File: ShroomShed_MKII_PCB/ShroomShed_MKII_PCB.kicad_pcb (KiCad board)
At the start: 4 copper layers, 91 x 72 mm, 92 parts, among them J1 TYPE-C-31-M-12, J2 UART, J3 Inputs, J4 SHT31, J5 SWD 14 pin header, J6 ERM, J7 SD_SPI, J8 Display_Touch_SPI, Q1 BC817, SW1 EVQ-Q2B03W, SW2 BOOT SELECT, U1 WS2811, U2 WS2811, U3 TPS61085DGK, U4 USBLC6-2SC6, U5 WS2811, U6 WS2811, U7 ENS210, U8 AMS1117-3.3, U9 STM32H562VGTx, Y1 16MHz

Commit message: completed controler V2.2, got basic blocking implementation of display SPI DMA working
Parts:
- removed the C12 at (173.7, 80.7)
- removed the R12 at (170.5, 77.9)
- removed the R13 at (176.4, 78.7)
- removed the U7 at (173.8, 78.4)
- added J10: GPIO_GND, Connector_PinHeader_2.54mm:PinHeader_2x02_P2.54mm_Vertical, F.Cu at (180.0, 67.2)
- added J4: GPIO_PWR, Connector_PinHeader_2.54mm:PinHeader_2x03_P2.54mm_Vertical, F.Cu at (169.2, 83.6)
- C14: renamed from C15; value 100uF -> 220uF
- H1, H2, H3, H4: footprint MountingHole:MountingHole_3.2mm_M3_Pad -> MountingHole:MountingHole_3.2mm_M3_Pad_Via
- J2: value UART -> GPIO_1; footprint Connector_PinHeader_2.00mm:PinHeader_1x04_P2.00mm_Vertical -> Connector_PinHeader_2.54mm:PinHeader_2x08_P2.54mm_Vertical
- J3: value Inputs -> GPIO_2; footprint Connector_JST:JST_XH_B6B-XH-A_1x06_P2.50mm_Vertical -> Connector_PinHeader_2.54mm:PinHeader_2x05_P2.54mm_Vertical
- moved D15 16.5 mm to (167.6, 61.0)
- moved R19 16.5 mm to (167.6, 63.0)
- moved J2 16.3 mm to (142.5, 74.0)
- moved J3 12.2 mm to (154.9, 83.6), turned to 90 degrees
- moved J6 9.90 mm to (181.7, 82.0)
- moved C2 9.01 mm to (173.0, 120.8)
- moved R1 9.01 mm to (173.0, 124.5)
- moved R3 9.01 mm to (173.0, 122.5)
- moved U1 9.01 mm to (167.2, 122.8)
- moved D1 9.01 mm to (177.8, 115.8)
- moved D2 9.01 mm to (172.0, 115.8)
- moved D3 9.01 mm to (166.2, 115.8)
- moved H1 9.00 mm to (181.0, 62.0)
- moved H3 9.00 mm to (181.0, 124.0)
- moved C15 8.62 mm to (175.6, 73.0), turned to -90 degrees
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- renumbered C13 to C12, C14 to C13, C16 to C15, C17 to C16, C18 to C17, C19 to C18, C20 to C19, C21 to C20, C22 to C21, C23 to C22, C24 to C23, C25 to C24, C26 to C25, C27 to C26, C28 to C27, J4 to J5, J5 to J7, J7 to J8, J8 to J9, R14 to R12, R15 to R13, R16 to R14, R17 to R15, R18 to R16, R19 to R17, R20 to R18, R21 to R19, U8 to U7, U9 to U8
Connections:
- J2 pad 1: +3V3 -> PA10
- J2 pad 2: RF_TX -> PA9
- J2 pad 3: RF_RX -> PC8
- J2 pad 4: GND -> PC7
- J3 pad 1: ENCODER_CHANNEL_A -> PB10
- J3 pad 2: ENCODER_CHANNEL_B -> PE15
- J3 pad 3: INPUT_1 -> PE14
- J3 pad 4: INPUT_2 -> PE13
- J3 pad 5: INPUT_3 -> PE12
- J3 pad 6: GND -> PE11
- U8 pad 38: RF_RX -> PE7
- U8 pad 39: RF_TX -> PE8
- U8 pad 40: unconnected-(U9-PE9-Pad40) -> PE9
- U8 pad 41: unconnected-(U9-PE10-Pad41) -> PE10
- U8 pad 42: unconnected-(U9-PE11-Pad42) -> PE11
- U8 pad 43: unconnected-(U9-PE12-Pad43) -> PE12
- U8 pad 44: unconnected-(U9-PE13-Pad44) -> PE13
- U8 pad 45: unconnected-(U9-PE14-Pad45) -> PE14
- U8 pad 46: unconnected-(U9-PE15-Pad46) -> PE15
- U8 pad 47: ENS210_SCL -> PB10
- U8 pad 51: ENS210_SDA -> PB12
- U8 pad 53: unconnected-(U9-PB14-Pad53) -> PB14
- U8 pad 54: unconnected-(U9-PB15-Pad54) -> PB15
- U8 pad 55: unconnected-(U9-PD8-Pad55) -> PD8
- U8 pad 56: INPUT_3 -> PD9
- U8 pad 57: INPUT_2 -> PD10
- U8 pad 58: INPUT_1 -> PD11
- U8 pad 59: ENCODER_CHANNEL_B -> PD12
- U8 pad 60: ENCODER_CHANNEL_A -> PD13
- U8 pad 61: unconnected-(U9-PD14-Pad61) -> PD14
- U8 pad 62: unconnected-(U9-PD15-Pad62) -> PD15
- U8 pad 63: unconnected-(U9-PC6-Pad63) -> PC6
- U8 pad 64: unconnected-(U9-PC7-Pad64) -> PC7
- U8 pad 65: unconnected-(U9-PC8-Pad65) -> PC8
- U8 pad 68: unconnected-(U9-PA9-Pad68) -> PA9
- U8 pad 69: unconnected-(U9-PA10-Pad69) -> PA10
- U8 pad 77: TOUCH_NSS -> unconnected-(U8-PA15(JTDI)-Pad77)
- U8 pad 93: unconnected-(U9-PB7-Pad93) -> TOUCH_NSS
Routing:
- net ENS210_SCL: track 39.8 -> 0.00 mm
- net ENS210_SDA: track 30.3 -> 0.00 mm
- net PE7: track 0.00 -> 26.5 mm, vias 0 -> 1
- net PB12: track 0.00 -> 26.0 mm
- net RGB_MOSI: track 75.0 -> 49.8 mm, vias 0 -> 2
- net PB15: track 0.00 -> 25.0 mm, vias 0 -> 1
- net PE9: track 0.00 -> 23.5 mm, vias 0 -> 1
- net PD9: track 0.00 -> 23.3 mm, vias 0 -> 1
- net INPUT_3: track 22.9 -> 0.00 mm
- net PE8: track 0.00 -> 22.8 mm
- net PB14: track 0.00 -> 22.5 mm
- net PD11: track 0.00 -> 21.5 mm, vias 0 -> 1
- net INPUT_2: track 21.1 -> 0.00 mm
- net PD8: track 0.00 -> 20.7 mm
- net PE11: track 0.00 -> 20.6 mm, vias 0 -> 1
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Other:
- board size 91 x 72 mm -> 82 x 72 mm
- board text added: "Controller V2.2"
- board text removed: "Controller V2.1"

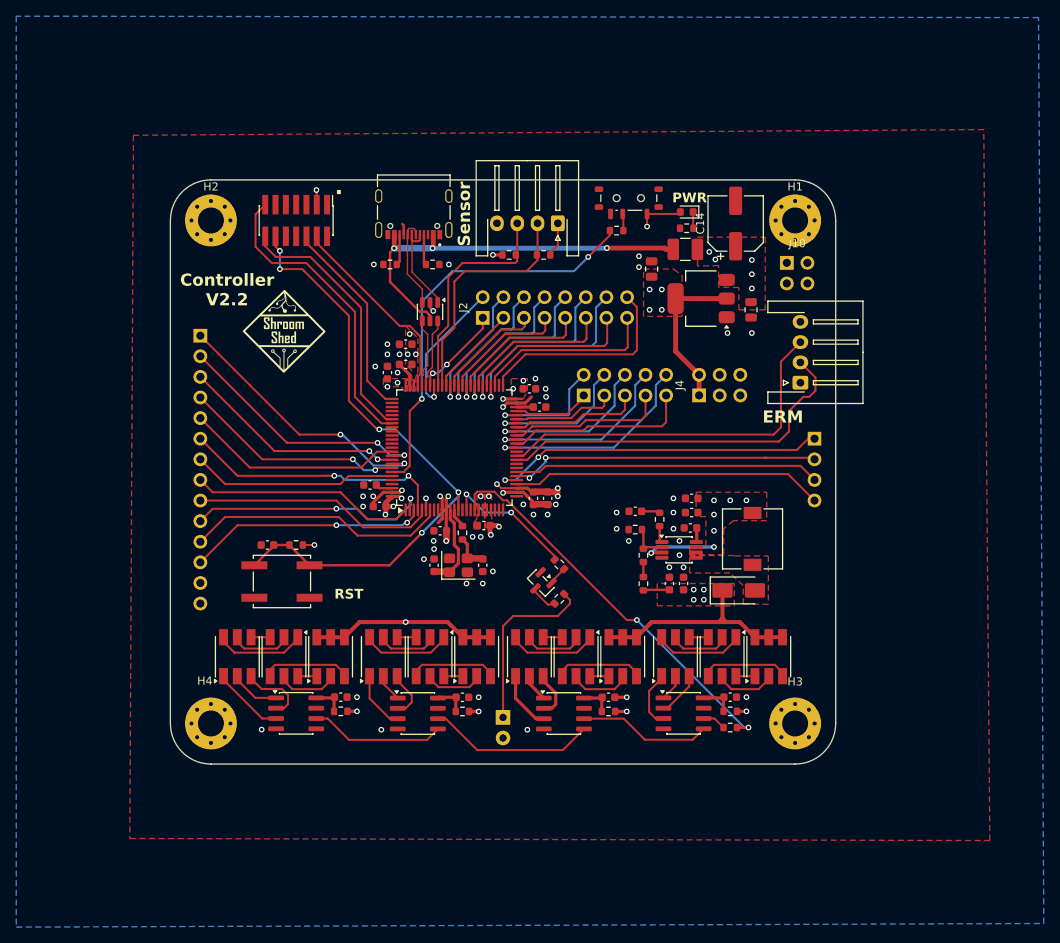
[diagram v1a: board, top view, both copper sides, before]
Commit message: Fixed distance between display pin headers, checkpoint for proper DMA implementation
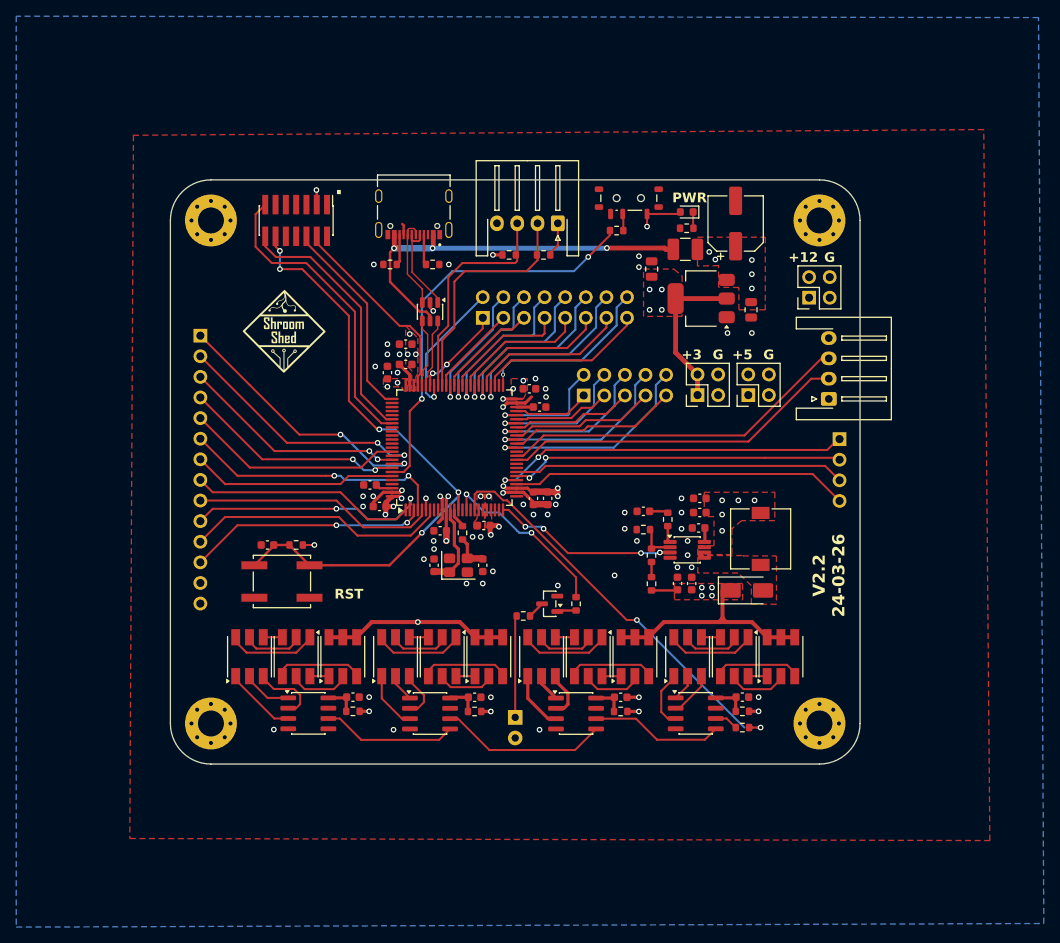
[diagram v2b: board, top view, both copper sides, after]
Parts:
- removed the J10 at (180.0, 67.2)
- added J5: 5V_PWR, Connector_PinHeader_2.54mm:PinHeader_2x02_P2.54mm_Vertical, F.Cu at (175.2, 83.5)
- added J6: 12V_PWR, Connector_PinHeader_2.54mm:PinHeader_2x02_P2.54mm_Vertical, F.Cu at (182.7, 71.5)
- J4: value GPIO_PWR -> 3V3_PWR; footprint Connector_PinHeader_2.54mm:PinHeader_2x03_P2.54mm_Vertical -> Connector_PinHeader_2.54mm:PinHeader_2x02_P2.54mm_Vertical
- moved R13 5.28 mm to (154.0, 109.2), turned to 90 degrees
- moved R14 4.92 mm to (147.5, 110.8), turned to 0 degrees
- moved J8 4.03 mm to (185.2, 84.0)
- moved J10 3.09 mm to (186.5, 89.0)
- moved H1 3.00 mm to (184.0, 62.0)
- moved H3 3.00 mm to (184.0, 124.0)
- moved Q1 2.79 mm to (150.8, 109.2), turned to 180 degrees
- moved C2 1.50 mm to (174.5, 120.8)
- moved C3 1.50 mm to (126.5, 120.8)
- moved C7 1.50 mm to (159.5, 120.8)
- moved C8 1.50 mm to (141.5, 120.8)
- moved D1 1.50 mm to (179.3, 115.8)
- moved D10 1.50 mm to (149.8, 115.8)
- moved D11 1.50 mm to (143.2, 115.8)
- moved D12 1.50 mm to (137.5, 115.8)
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- renumbered J8 to J10, J9 to J11, J5 to J7, J6 to J8, J7 to J9
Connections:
- J4 pad 3: +5V -> GND
- J4 pad 4: +5V -> GND
- U3 pad 3: +5V -> BOOST_EN
- U8 pad 25: unconnected-(U8-PA2-Pad25) -> BOOST_EN
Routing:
- net BOOST_EN: track 0.00 -> 22.8 mm, vias 0 -> 4
- net Net-(D14-K): track 22.1 -> 12.5 mm
- net +5V: track 9.43 -> 0.00 mm, vias 12 -> 10
- net WATER_LED: track 16.4 -> 22.1 mm
- net PB12: track 26.0 -> 22.3 mm, vias 0 -> 1
- net TRANSDUCER_PWM: track 46.2 -> 42.6 mm
- net SD_NSS: track 38.6 -> 41.7 mm
- net SD_MOSI: track 37.7 -> 40.8 mm
- net SD_SCK: track 41.7 -> 44.7 mm
- net SD_MISO: track 38.5 -> 41.3 mm
- net FAN_PWM: track 45.5 -> 43.4 mm
- net PE8: track 22.8 -> 20.9 mm
- net PB14: track 22.5 -> 20.9 mm
- net PE10: track 19.4 -> 17.9 mm
- net Net-(Q1-C): track 3.51 -> 2.12 mm
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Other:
- board size 82 x 72 mm -> 85 x 72 mm
- board text added: "+12"
- board text added: "+3"
- board text added: "+5"
- board text added: "G"
- board text added: "V2.2 24-03-26"
- board text removed: "Controller V2.2"
- board text removed: "ERM"
- board text removed: "Sensor"

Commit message: Controller V2.2 ordered
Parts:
- moved H1 3.00 mm to (187.0, 62.0)
- moved H3 3.00 mm to (187.0, 124.0)
- moved J8 2.50 mm to (187.7, 84.0)
- moved C1 2.37 mm to (171.5, 95.5)
- moved C10 2.37 mm to (170.5, 106.0)
- moved C4 2.37 mm to (171.5, 97.2)
- moved C5 2.37 mm to (171.3, 99.2)
- moved C6 2.37 mm to (164.6, 97.1)
- moved C9 2.37 mm to (168.8, 106.0)
- moved D7 2.37 mm to (177.3, 106.9)
- moved L1 2.37 mm to (179.0, 100.5)
- moved R5 2.37 mm to (167.6, 98.1)
- moved R7 2.37 mm to (165.5, 106.0)
- moved R8 2.37 mm to (164.6, 99.3)
- moved R9 2.37 mm to (165.5, 102.5)
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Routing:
- net RGB_MOSI: track 49.3 -> 52.2 mm
- net TRANSDUCER_PWM: track 42.6 -> 45.1 mm
- net FAN_PWM: track 43.4 -> 45.9 mm
- net SD_SCK: track 44.7 -> 47.0 mm
- net SD_NSS: track 41.7 -> 43.7 mm
- net SD_MOSI: track 40.8 -> 42.9 mm
- net SD_MISO: track 41.3 -> 43.3 mm
- net BOOST_EN: track 22.8 -> 24.8 mm
- net +12V: track 59.7 -> 60.7 mm
- net WATER_LED: track 22.1 -> 22.7 mm
- net +5V: vias 10 -> 9
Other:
- board size 85 x 72 mm -> 88 x 72 mm
- board text added: "Controller V2.2"
- board text removed: "V2.2 24-03-26"
